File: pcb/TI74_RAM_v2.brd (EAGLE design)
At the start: 25.4 x 27 mm, 11 parts, among them IC1 JEDEC_32KB_SRAM, X1 TI74_CONN

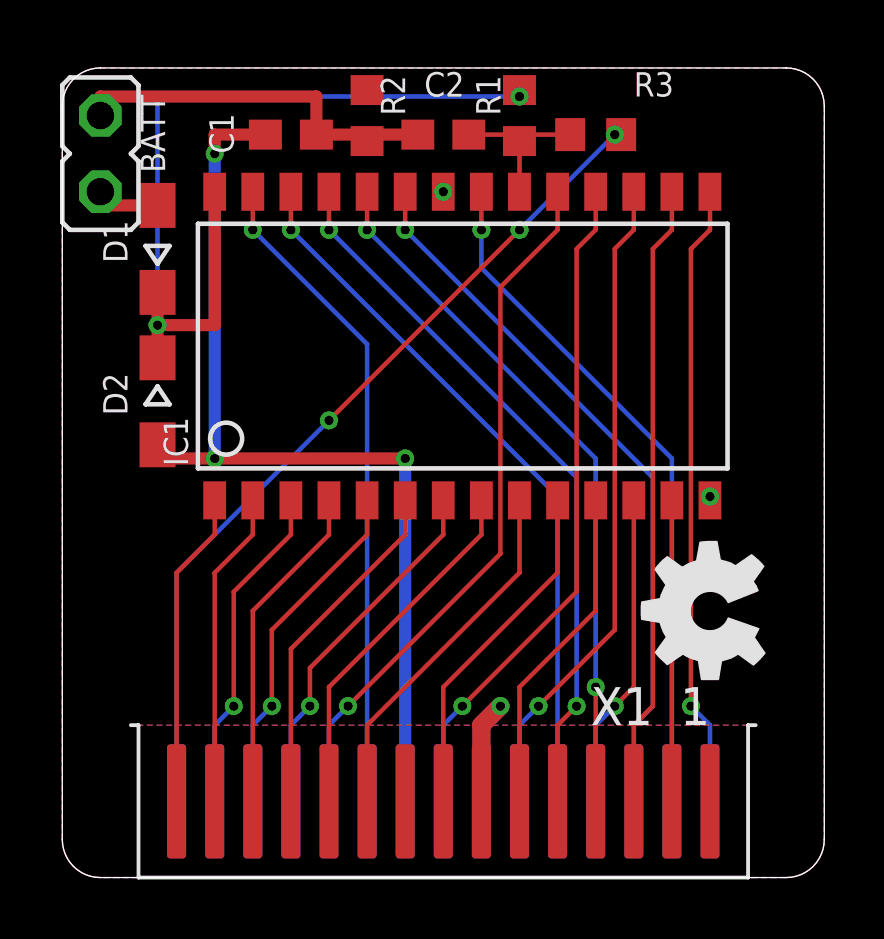
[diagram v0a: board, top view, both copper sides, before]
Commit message: Fixed A15->A0 mistake and shortened board (v2)
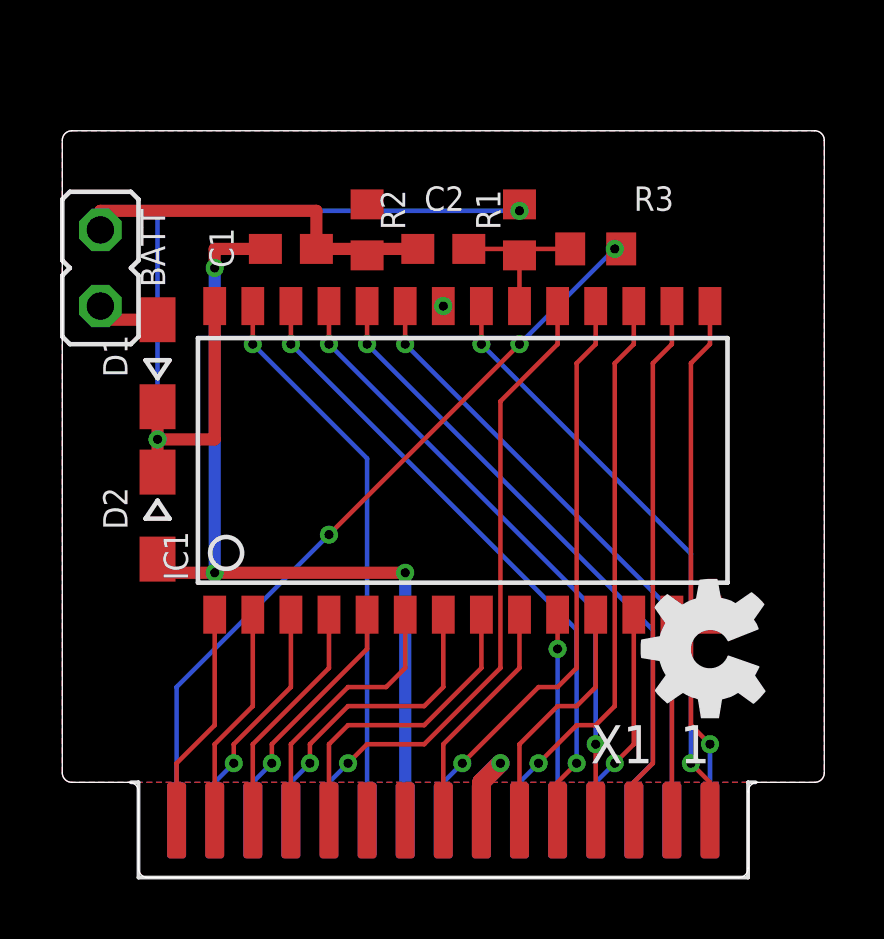
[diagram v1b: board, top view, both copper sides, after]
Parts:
- IC1: value JEDEC_32KB_SRAM -> IS62C256
- moved C1 3.81 mm to (-5.08, 21.0)
- moved C2 3.81 mm to (0.00, 21.0)
- moved R3 3.81 mm to (5.08, 21.0)
- moved D2 3.81 mm to (-9.53, 12.1)
- moved IC1 3.81 mm to (0.00, 14.0)
- moved BATT 3.81 mm to (-11.4, 20.3)
- moved D1 3.81 mm to (-9.53, 17.1)
- moved R1 3.81 mm to (2.54, 21.6)
- moved R2 3.81 mm to (-2.54, 21.6)
- moved GOLD_ORB_SM1 1.27 mm to (8.89, 7.62)
- moved X1 0.64 mm to (0.00, 1.91)
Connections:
- net A0: now also IC1.21
- net A1: now also IC1.25; no longer IC1.24
- net A10: now also IC1.24; no longer IC1.23
- net A11: now also IC1.23; no longer IC1.21
- net A12: now also IC1.10; no longer IC1.26
- net A15: no longer IC1.9
- net A2: now also IC1.26; no longer IC1.25
- net A3: now also IC1.9; no longer IC1.10
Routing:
- net A0: track 0.00 -> 20.3 mm, vias 0 -> 2
- net A12: track 24.0 -> 6.86 mm
- net A15: track 12.1 -> 0.00 mm
- net A3: track 11.6 -> 7.91 mm
- net D3: track 10.6 -> 7.38 mm
- net D0: track 10.0 -> 6.86 mm
- net D7: track 20.8 -> 17.7 mm
- net D1: track 20.8 -> 17.7 mm
- net A9: track 11.6 -> 8.44 mm
- net A7: track 10.6 -> 7.38 mm
- net A6: track 10.6 -> 7.38 mm
- net A14: track 11.1 -> 7.91 mm
- net A13: track 11.1 -> 7.91 mm
- net R/!W: track 21.9 -> 18.7 mm
- net N$2: track 32.8 -> 29.6 mm
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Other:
- board size 25.4 x 27 mm -> 25.4 x 24.9 mm
